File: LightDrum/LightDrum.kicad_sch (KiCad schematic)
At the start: 22 parts, among them J102 JTAG, Q101 RQ5A030AP, SW101 BOOT1, SW102 BOOT0, U101 TCAN1044, U102 24LC04, Y101 8MHz

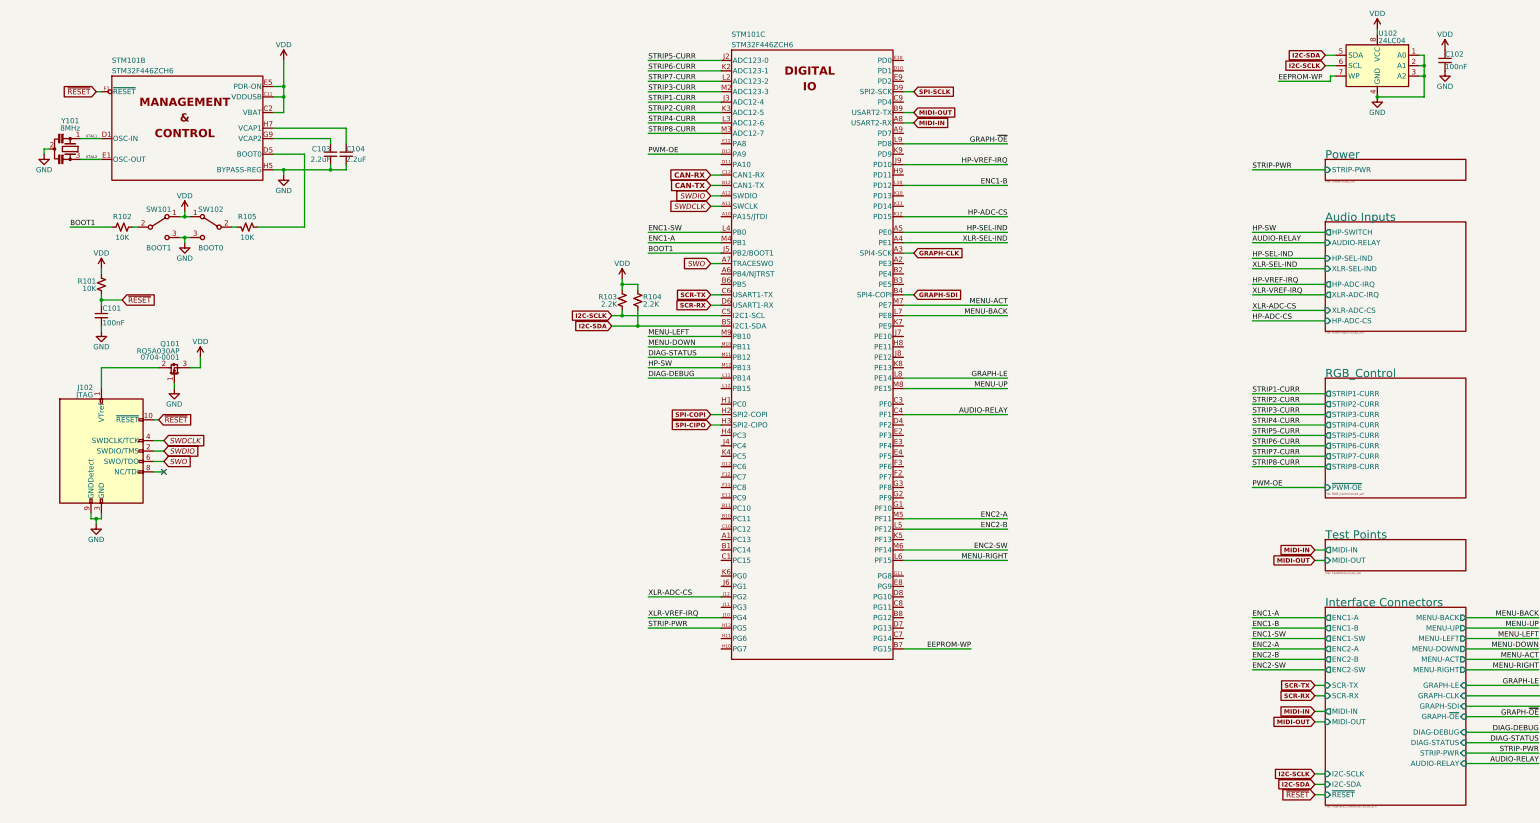
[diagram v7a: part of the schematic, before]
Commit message: Replace old MCU W/ STM32F412
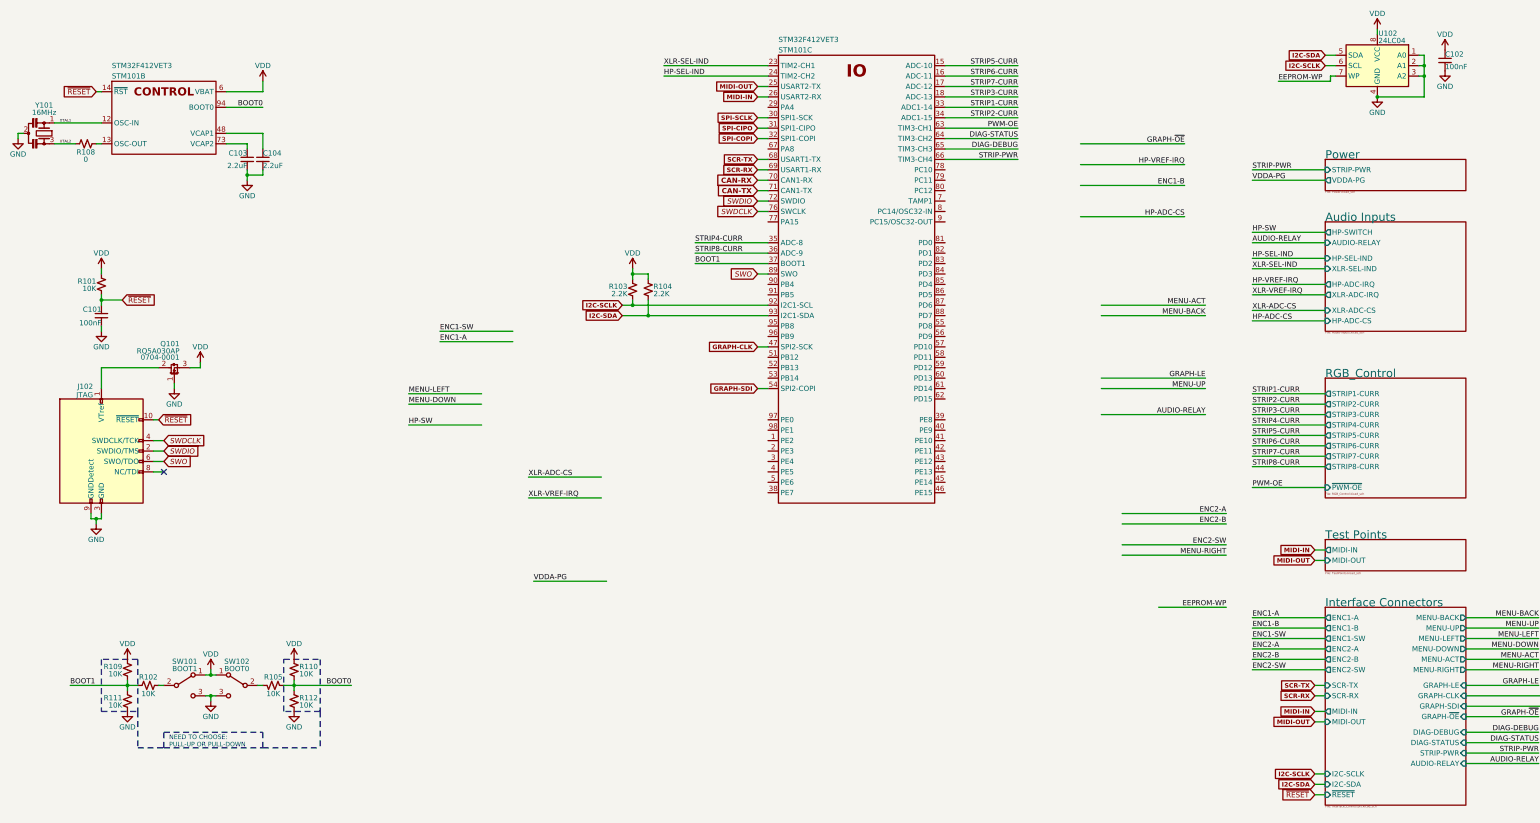
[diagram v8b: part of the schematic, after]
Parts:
- removed STM101: STM32F446ZCH6, Daxxn_Packages:UFBGA144-7x7xOP6, symbol Daxxn_STMicros:STM32F446ZCH6
- added R108: 0, Resistor_SMD:R_0402_1005Metric, symbol Device:R_Small_US
- added R109, R110, R111, R112: 10K, Resistor_SMD:R_0402_1005Metric, symbol Device:R_Small_US
- added STM101: STM32F412VET3, Package_QFP:LQFP-100_14x14mm_P0.5mm, symbol Daxxn_STMicros:STM32F412VET3
- Y101: value 8MHz -> 16MHz
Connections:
- net BOOT1: now also R109.2, R111.1, STM101.37 (PB2)
- net CAN-RX: now also STM101.70 (PA11)
- net CAN-TX: now also STM101.71 (PA12)
- net DIAG-DEBUG: now also STM101.65 (PC8)
- net DIAG-STATUS: now also STM101.64 (PC7)
- net GND: now also R111.2, R112.2
- net GRAPH-CLK: now also STM101.47 (PB10)
- net GRAPH-SDI: now also STM101.54 (PB15)
- net HP-SEL-IND: now also STM101.24 (PA1)
- net I2C-SCLK: now also STM101.92 (PB6)
- net I2C-SDA: now also STM101.93 (PB7)
- net MIDI-IN: now also STM101.26 (PA3)
- net MIDI-OUT: now also STM101.25 (PA2)
- net PWM-OE: now also STM101.63 (PC6)
- net SCR-RX: now also STM101.69 (PA10)
- net SCR-TX: now also STM101.68 (PA9)
- net SPI-CIPO: now also STM101.31 (PA6)
- net SPI-COPI: now also STM101.32 (PA7)
- net SPI-SCLK: now also STM101.30 (PA5)
- net STRIP-PWR: now also STM101.66 (PC9)
- net STRIP1-CURR: now also STM101.33 (PC4)
- net STRIP2-CURR: now also STM101.34 (PC5)
- net STRIP3-CURR: now also STM101.18 (PC3)
- net STRIP4-CURR: now also STM101.35 (PB0)
- net STRIP5-CURR: now also STM101.15 (PC0)
- net STRIP6-CURR: now also STM101.16 (PC1)
- net STRIP7-CURR: now also STM101.17 (PC2)
- net STRIP8-CURR: now also STM101.36 (PB1)
- net SWDCLK: now also STM101.76 (PA14)
- net SWDIO: now also STM101.72 (PA13)
- net SWO: now also STM101.89 (PB3)
- net VDD: now also R109.1, R110.1, STM101.6 (VBAT)
- net XLR-SEL-IND: now also STM101.23 (PA0)
- net XTAL1: now also STM101.12 (OSC-IN)
- net XTAL2: now also R108.2
- net ~{RESET}: now also STM101.14 (~{RST})
- net BOOT0: now reaches R105.2
- net BOOT0: now also R110.2, R112.1, STM101.94 (BOOT0)
- net at C104.1: now also STM101.48 (VCAP1)
- net at C103.1: now also STM101.73 (VCAP2)
- new net: R108.1, STM101.13 (OSC-OUT)
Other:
- sheet Power ports: added VDDA-PG; removed none
- note added: "NEED TO CHOOSE: PULL-UP OR PULL-DOWN"
- moved on the sheet: C103, C104, R102, R103, R104, R105, SW101, SW102, Y101
